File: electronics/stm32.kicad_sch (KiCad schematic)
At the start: 38 parts, among them J1 USB_B_Micro, J2 Conn_ARM_JTAG_SWD_10, SW1 PTS645SK50SMTR92LFS, U1 USBLC6-2SC6, U2 STM32F446RETx, Y1 Crystal_GND24

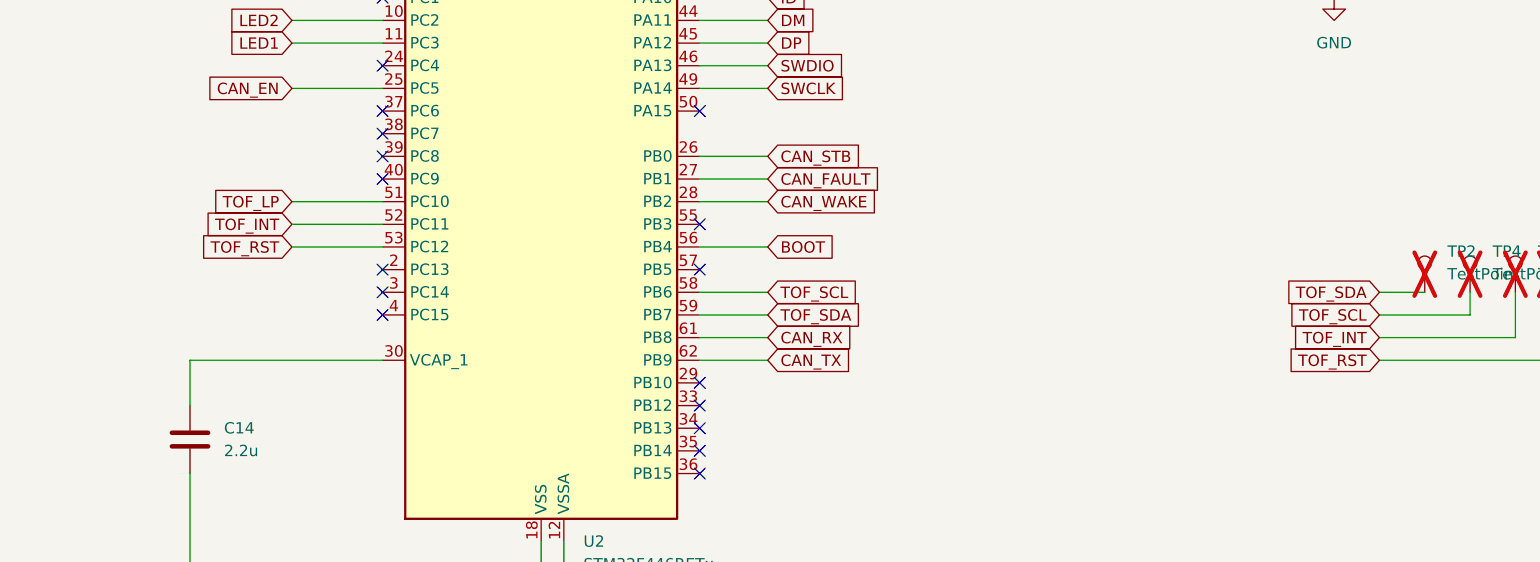
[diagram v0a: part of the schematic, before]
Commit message: Switched to a lower cost TOF sensor.
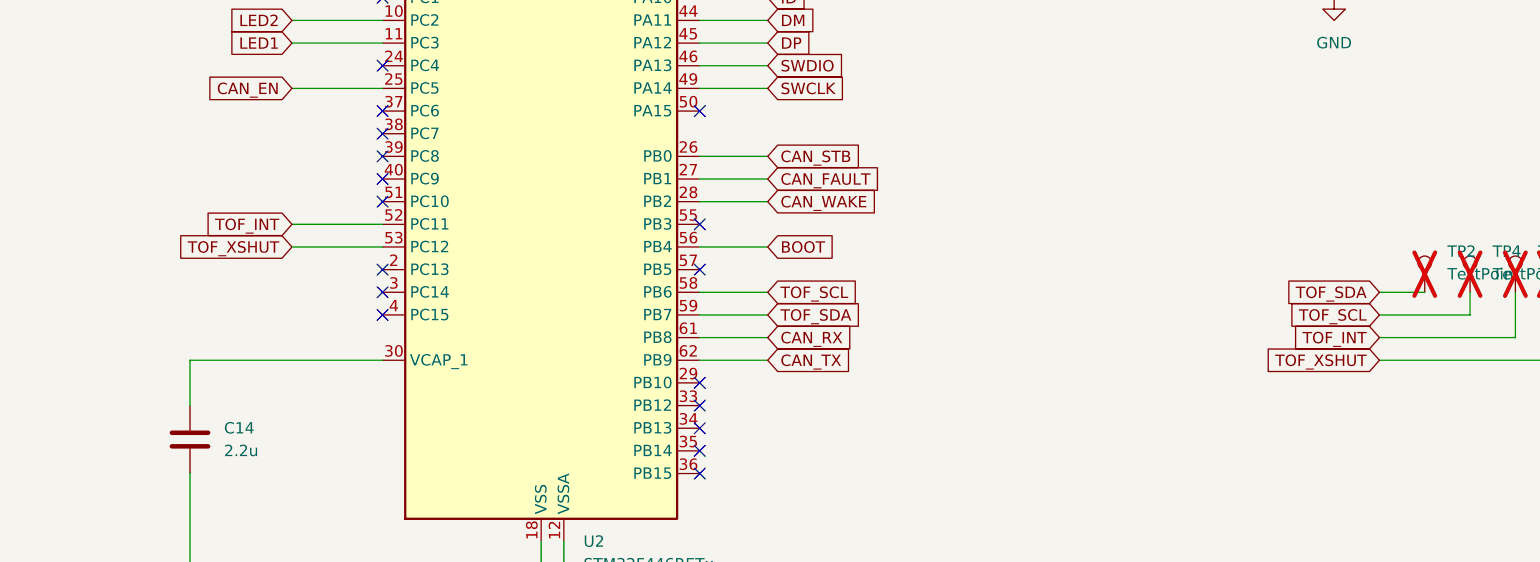
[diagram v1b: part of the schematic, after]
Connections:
- net TOF_LP: no longer names the net of U2.51 (PC10)
- net TOF_RST renamed TOF_XSHUT
- no-connect marks 30 -> 31
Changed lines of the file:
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@@
+	)
+	(no_connect
+		(at 134.62 110.49)
 	)
 	(no_connect
@@
 	(wire
 		(pts
-			(xy 124.46 110.49) (xy 134.62 110.49)
-		)
-		(stroke
-			(width 0)
-			(type default)
-		)
-	)
-	(wire
-		(pts
 			(xy 106.68 175.26) (xy 95.25 175.26)
 		)
@@
 	(wire
 		(pts
+			(xy 124.46 115.57) (xy 134.62 115.57)
+		)
+		(stroke
+			(width 0)
+			(type default)
+		)
+	)
+	(wire
+		(pts
 			(xy 44.45 53.34) (xy 44.45 64.77)
 		)
@@
 		(pts
 			(xy 154.94 160.02) (xy 154.94 162.56)
-		)
-		(stroke
-			(width 0)
-			(type default)
-		)
-	)
-	(wire
-		(pts
-			(xy 124.46 115.57) (xy 134.62 115.57)
 		)
 		(stroke
@@
 		)
 	)
-	(global_label "TOF_RST"
+	(global_label "TOF_XSHUT"
 		(shape input)
 		(at 246.38 128.27 180)
@@
 		)
 		(property "Intersheetrefs" "${INTERSHEET_REFS}"
-			(at 235.5934 128.27 0)
+			(at 232.9929 128.27 0)
 			(effects
 				(font
@@
 		)
 	)
-	(global_label "TOF_RST"
+	(global_label "TOF_XSHUT"
 		(shape input)
 		(at 124.46 115.57 180)
@@
 		)
 		(property "Intersheetrefs" "${INTERSHEET_REFS}"
-			(at 113.6734 115.57 0)
+			(at 111.0729 115.57 0)
 			(effects
 				(font
@@
 			(effects
 				(font
-					(size 1.27 1.27)
-				)
-				(justify right)
-				(hide yes)
-			)
-		)
-	)
-	(global_label "TOF_LP"
-		(shape input)
-		(at 124.46 110.49 180)
-		(fields_autoplaced yes)
-		(effects
-			(font
-				(size 1.27 1.27)
-			)
-			(justify right)
-		)
-		(property "Intersheetrefs" "${INTERSHEET_REFS}"
-			(at 114.8224 110.49 0)
-			(effects
-				(font

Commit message: Ordered this version.
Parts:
- removed C11, C12, C13, C15: 0.1u, Capacitor_SMD:C_0402_1005Metric, symbol Device:C
- removed C14: 2.2u, Capacitor_SMD:C_0603_1608Metric, symbol Device:C
- removed U2: STM32F446RETx, Package_QFP:LQFP-64_10x10mm_P0.5mm, symbol MCU_ST_STM32F4:STM32F446RETx
- added U2: STM32G431CBUx, Package_DFN_QFN:QFN-48-1EP_7x7mm_P0.5mm_EP5.6x5.6mm, symbol MCU_ST_STM32G4:STM32G431CBUx
- C1: footprint Capacitor_SMD:C_0805_2012Metric -> Capacitor_SMD:C_0603_1608Metric; JLCPCB (none) -> C1705
- R1: footprint Resistor_SMD:R_0603_1608Metric -> Resistor_SMD:R_0402_1005Metric; JLCPCB (none) -> C25126
- R2, R6: JLCPCB (none) -> C11702
- renumbered R9 to R8, R10 to R9, TP2 to TP1, TP4 to TP2, TP5 to TP3, TP6 to TP4, TP7 to TP5
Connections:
- net BOOT: now also U2.13 (PA5)
- net CAN_RX: now also U2.46 (PB8)
- net CAN_STB: now also U2.2 (PC13)
- net CAN_TX: now also U2.47 (PB9)
- net DM: now also U2.33 (PA11)
- net DP: now also U2.34 (PA12)
- net GND: now also U2.49 (VSS)
- net ID: now also U2.32 (PA10)
- net LED1: now also U2.15 (PA7)
- net LED2: now also U2.14 (PA6)
- net NRST: now also U2.7 (PG10)
- net OSC_IN: now also U2.5 (PF0)
- net SWCLK: now also U2.37 (PA14)
- net SWDIO: now also U2.36 (PA13)
- net TOF_INT: now also U2.43 (PB5)
- net TOF_SCL: now also U2.38 (PA15)
- net TOF_SDA: now also U2.45 (PB7)
- net TOF_XSHUT: now also U2.44 (PB6)
- net VIN_MEAS: now also U2.8 (PA0)
- net at R6.1: now also U2.6 (PF1)
- net +3.3V renamed 3V3
- net 3V3: now also U2.1 (VBAT), U2.20 (VREF+), U2.21 (VDDA), U2.23 (VDD), U2.35 (VDD), U2.48 (VDD)
- no-connect marks 31 -> 27
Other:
- moved on the sheet: R7

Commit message: Major refactor to rev B
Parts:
- removed C5, C6, C7: 0.1u, Capacitor_SMD:C_0402_1005Metric, symbol Device:C
- removed J1: USB_B_Micro, Connector_USB:USB_Micro-B_Amphenol_10118193-0001LF_Horizontal, symbol Connector:USB_B_Micro
- removed R1: 560, Resistor_SMD:R_0402_1005Metric, symbol Device:R
- removed TP2, TP3, TP4: TestPoint, TestPoint:TestPoint_Pad_D1.0mm, symbol Connector:TestPoint
- removed U2: STM32G431CBUx, Package_DFN_QFN:QFN-48-1EP_7x7mm_P0.5mm_EP5.6x5.6mm, symbol MCU_ST_STM32G4:STM32G431CBUx
- added J5: USB_C_Receptacle, footprints:CONN_105450-0101_MOL, symbol Connector:USB_C_Receptacle
- added TP10, TP11, TP12, TP13, TP14, TP6, TP7, TP8, TP9: TestPoint, TestPoint:TestPoint_Pad_D1.0mm, symbol Connector:TestPoint
- added U9: STM32G0B1KBUx, Package_DFN_QFN:QFN-32-1EP_5x5mm_P0.5mm_EP3.45x3.45mm, symbol MCU_ST_STM32G0:STM32G0B1KBUx
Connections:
- net SWCLK is gone; now on net BOOT: J2.4 (SWCLK/TCK)
- net 3V3: now also U9.4 (VDD)
- net BOOT: now also U9.25 (PA14), U9.9 (PA2)
- net CAN_RX: now also U9.32 (PB8)
- net CAN_STB: now also U9.10 (PA3)
- net CAN_TX: now also U9.1 (PB9)
- net DM: now also U9.22 (PA9/PA11)
- net DP: now also U9.23 (PA10/PA12)
- net GND: now also TP1.1, J5.A1 (GND), J5.A12 (GND), J5.B1 (GND), J5.B12 (GND), U9.33 (VSS), U9.5 (VSS); no longer TP5.1
- net LED1: now also TP13.1, U9.8 (PA1)
- net LED2: now also TP14.1, U9.18 (PA8)
- net NRST: now also U9.6 (PF2)
- net OSC_IN: now also U9.2 (PC14)
- net SWDIO: now also U9.24 (PA13)
- net TOF_INT: now also TP6.1, U9.15 (PB0)
- net TOF_SCL: now also TP7.1, U9.19 (PA9/UCPD1_DBCC1)
- net TOF_SDA: now also TP8.1, U9.13 (PA6); no longer TP1.1
- net TOF_XSHUT: now also TP5.1, U9.16 (PB1)
- net VIN_MEAS: now also U9.7 (PA0)
- net at R5.1: now also U1.4 (I/O2); no longer U1.6 (I/O1)
- net at C4.2, D1.2 (A): now also J5.A4 (VBUS), J5.A9 (VBUS), J5.B4 (VBUS), J5.B9 (VBUS)
- net at R6.1: now also U9.3 (PC15)
- net at U1.1 (I/O1): now also J5.A6 (D+), J5.B6 (D+)
- net at U1.3 (I/O2): now also J5.A7 (D-), J5.B7 (D-)
- net at R4.1: now also U1.6 (I/O1); no longer U1.4 (I/O2)
- new net TB_CLK: TP12.1, U9.27 (PB3)
- new net TB_CS: TP9.1, U9.20 (PC6), U9.26 (PA15)
- new net TB_MISO: TP11.1, U9.28 (PB4), U9.30 (PB6)
- new net TB_MOSI: TP10.1, U9.29 (PB5)
- no-connect marks 27 -> 23
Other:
- moved on the sheet: C4, D1, D2, D3, J2, R4, R5, R7, R8, R9, U1

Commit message: Refactored the design to use basic parts.
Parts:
- C1: JLCPCB C1705 -> C19666
- R3: JLCPCB C102750 -> C25741
- R4, R5: JLCPCB C25152 -> C25092
- R7: JLCPCB C103059 -> C25900
- R8, R9: JLCPCB C12246 -> C25104
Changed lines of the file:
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@@
 			)
 		)
-		(property "JLCPCB" "C25152"
+		(property "JLCPCB" "C25092"
 			(at 104.14 35.56 0)
 			(effects
@@
 			)
 		)
-		(property "JLCPCB" "C12246"
+		(property "JLCPCB" "C25104"
 			(at 256.54 30.48 0)
 			(effects
@@
 			)
 		)
-		(property "JLCPCB" "C12246"
+		(property "JLCPCB" "C25104"
 			(at 256.54 39.37 0)
 			(effects
@@
 			)
 		)
-		(property "JLCPCB" "C103059"
+		(property "JLCPCB" "C25900"
 			(at 132.08 57.15 0)
 			(effects
@@
 			)
 		)
-		(property "JLCPCB" "C102750"
+		(property "JLCPCB" "C25741"
 			(at 67.31 138.43 0)
 			(effects
@@
 			)
 		)
-		(property "JLCPCB" "C1705"
+		(property "JLCPCB" "C19666"
 			(at 19.05 181.61 0)
 			(effects
@@
 			)
 		)
-		(property "JLCPCB" "C25152"
+		(property "JLCPCB" "C25092"
 			(at 104.14 33.02 0)
 			(effects

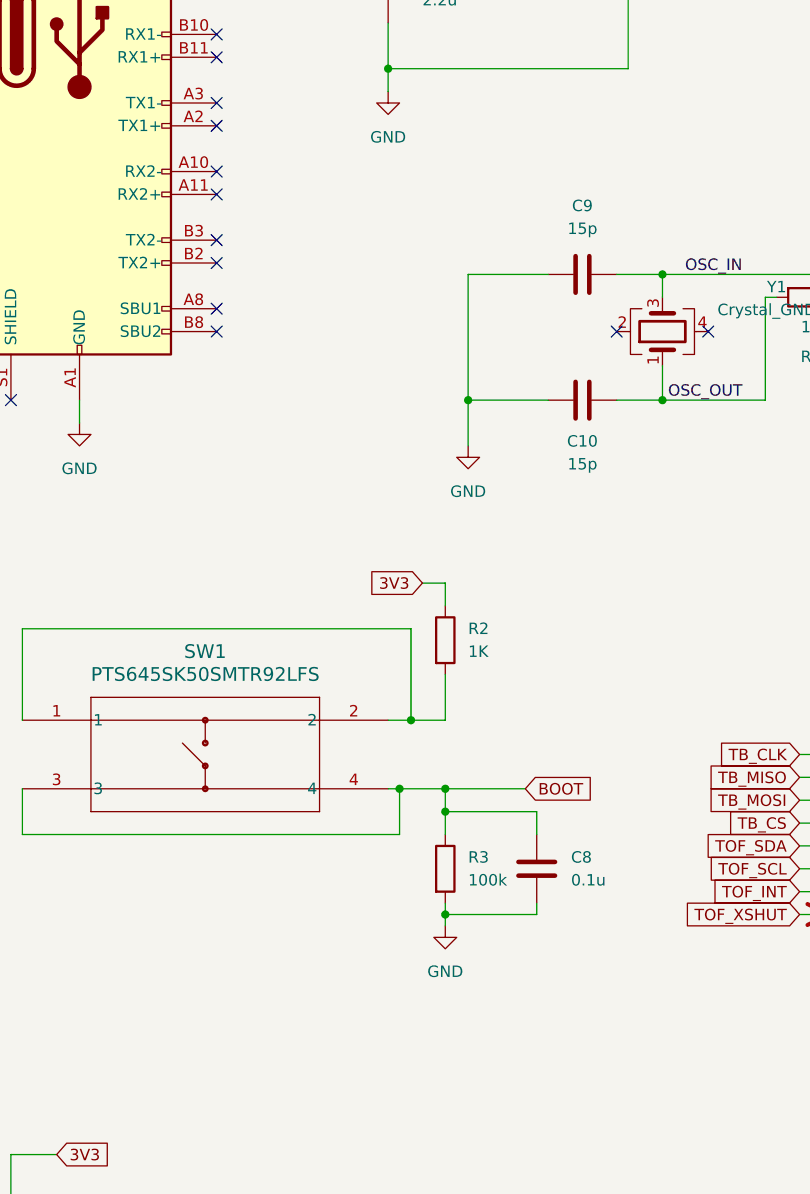
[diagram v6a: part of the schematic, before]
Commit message: Updated to the latest STM32CubeMX and now using STM32CubeIDE for VS Code.
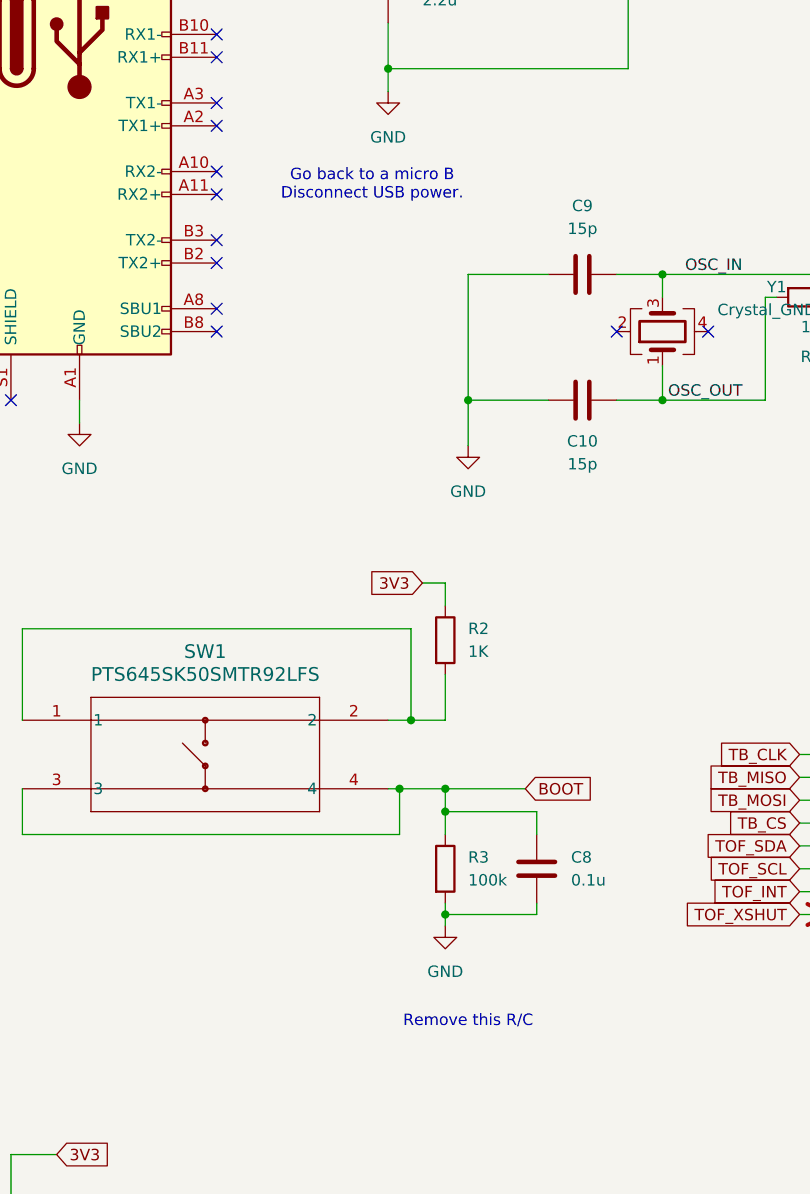
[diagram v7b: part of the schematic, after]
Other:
- note added: "Go back to a micro B Disconnect USB power."
- note added: "Remove this R/C"
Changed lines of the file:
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@@
 	(generator_version "9.0")
 	(paper "A4")
+	(text "Remove this R/C"
+		(exclude_from_sim no)
+		(at 69.85 155.448 0)
+		(effects
+			(font
+				(size 1.27 1.27)
+			)
+		)
+	)
+	(text "Go back to a micro B\nDisconnect USB power."
+		(exclude_from_sim no)
+		(at 59.182 62.484 0)
+		(effects
+			(font
+				(size 1.27 1.27)
+			)
+		)
+	)
 	(junction
 		(at 264.16 30.48)
